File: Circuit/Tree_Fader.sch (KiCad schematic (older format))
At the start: 20 parts

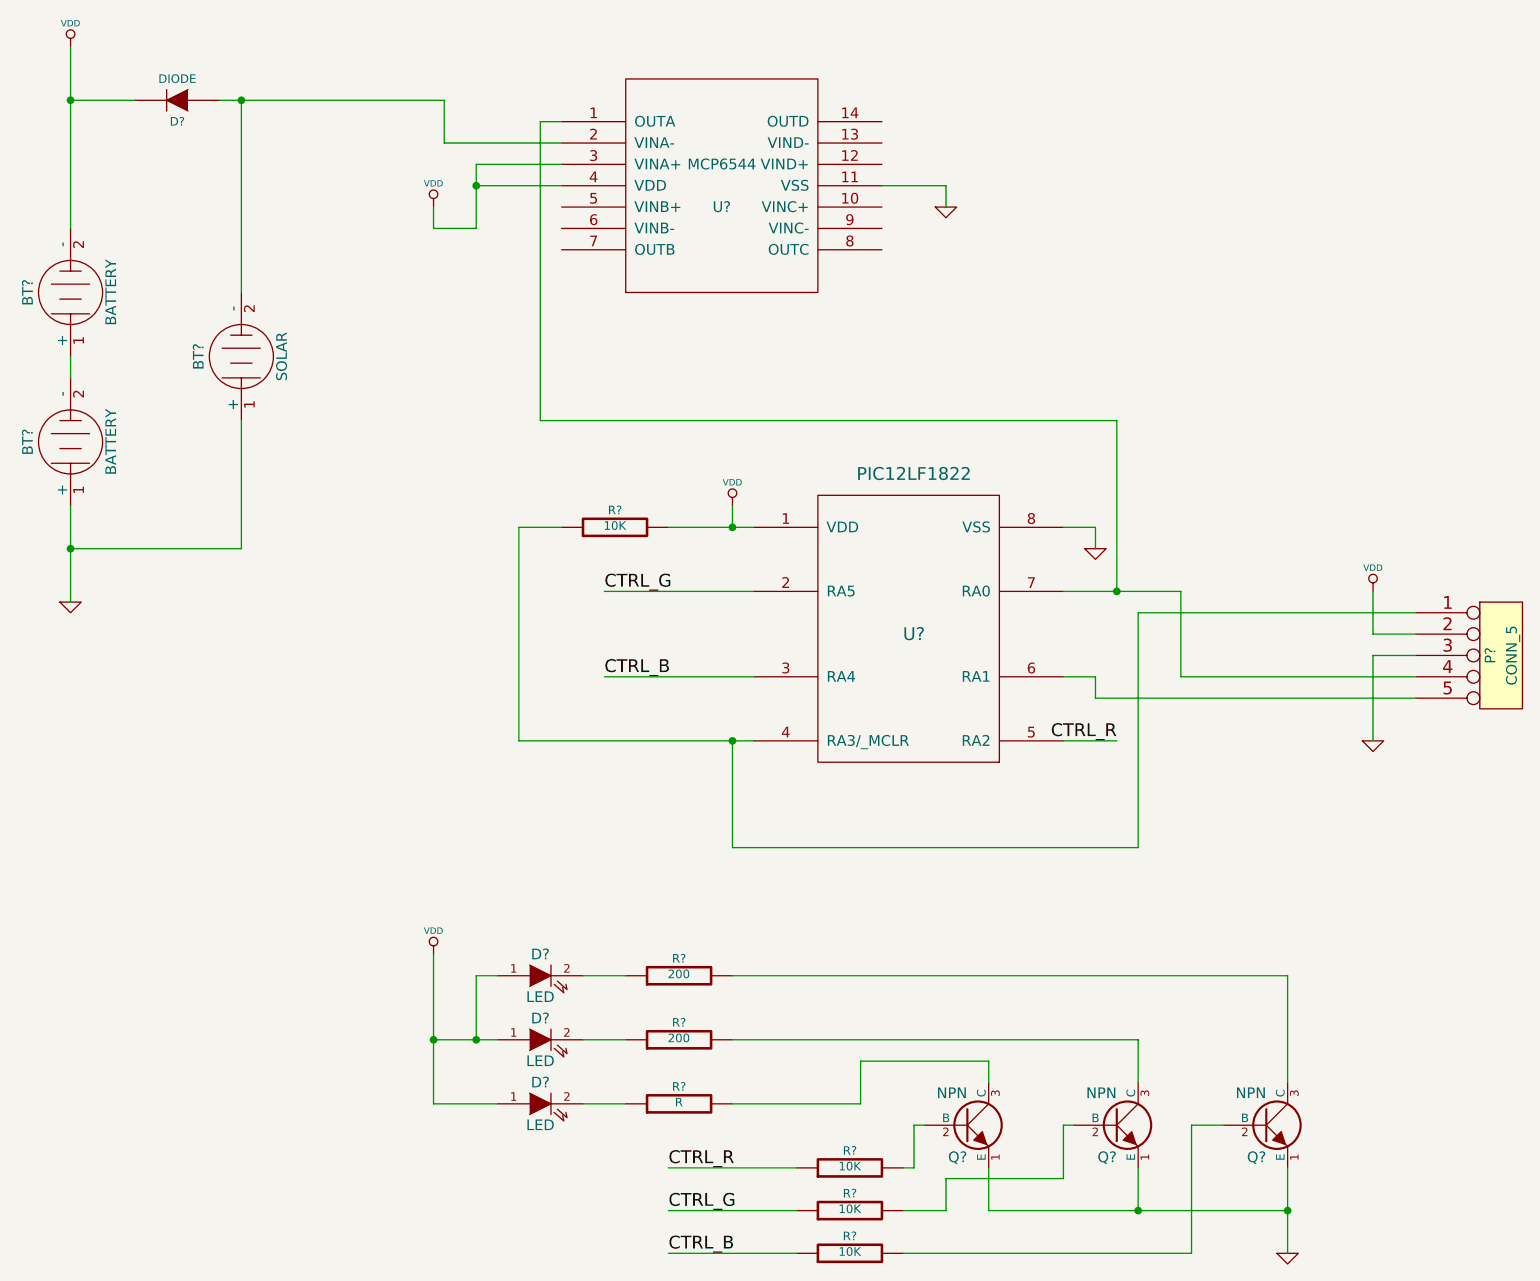
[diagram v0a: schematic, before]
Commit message: Created PCB in KiCad
Submitted order to OSH Park.  Of course, resistors R4 and R3 are not
connected to the ground of D4 and D3.  This is fixed here, but the order
was submitted, and will require a "bodge wire".
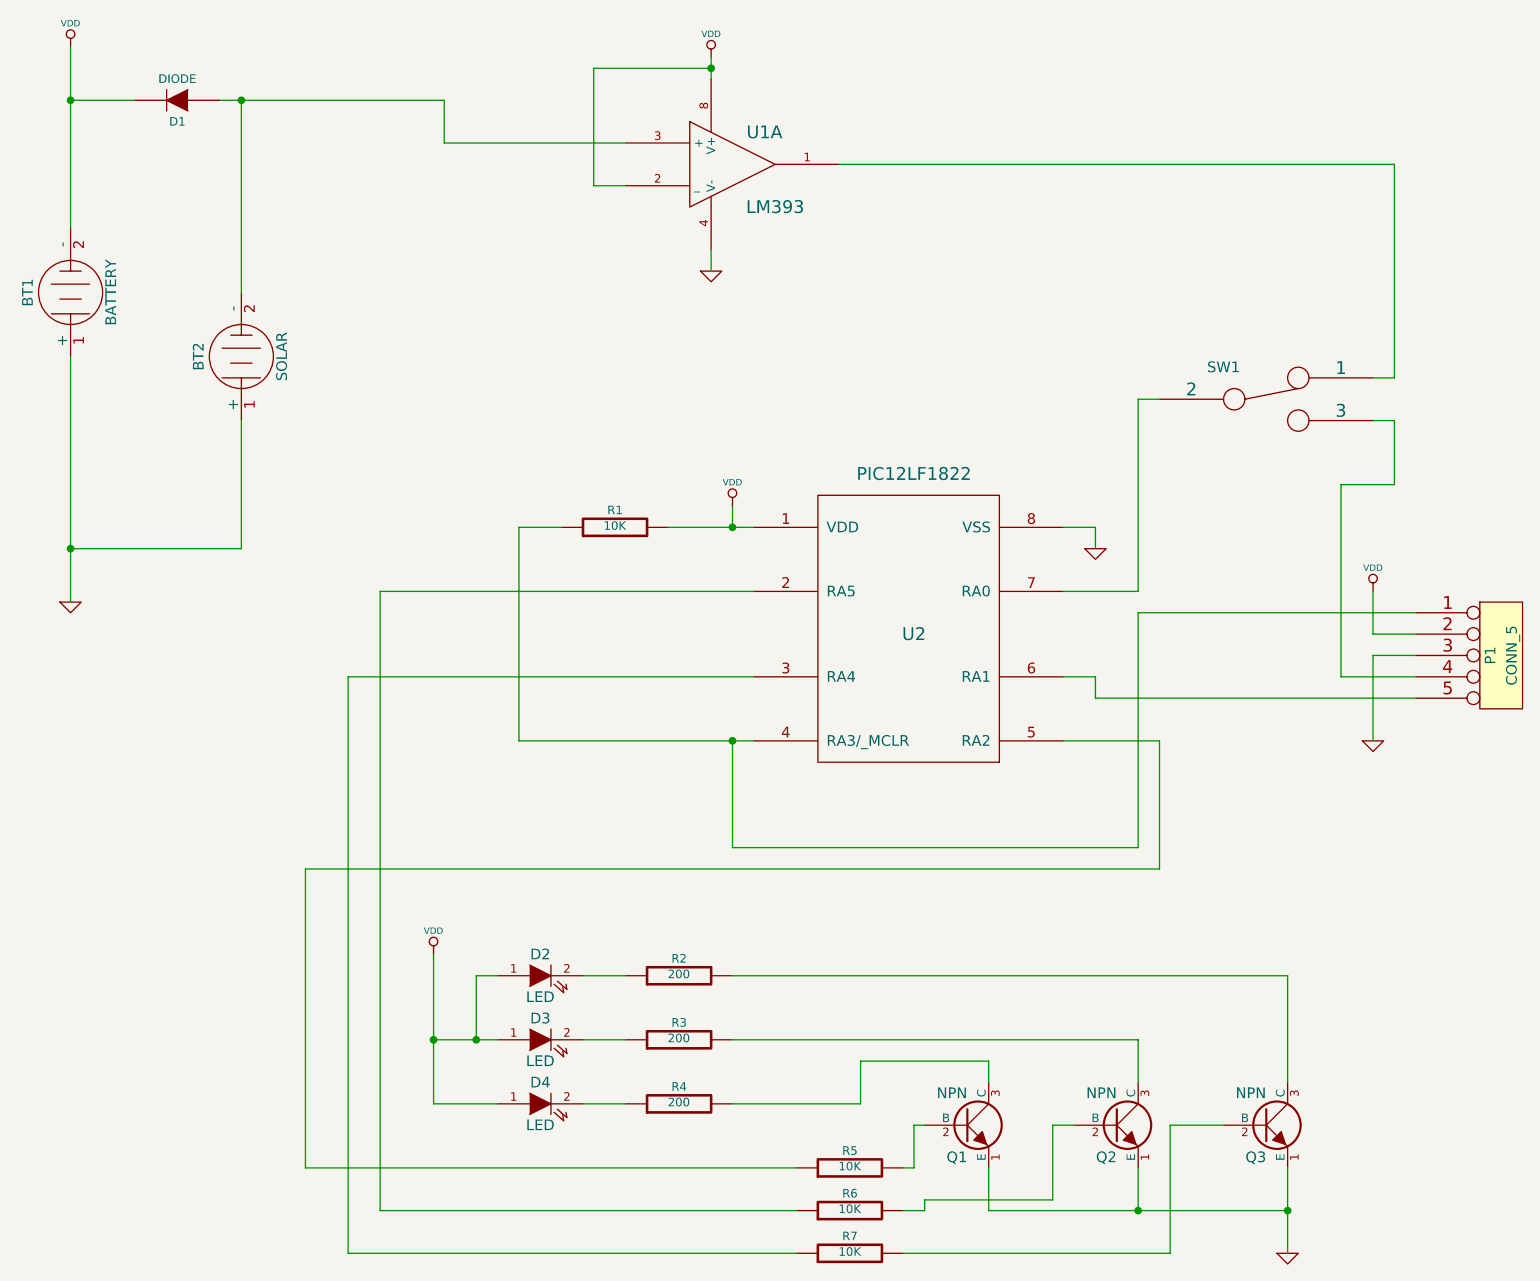
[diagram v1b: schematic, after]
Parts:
- removed BT?: BATTERY, ~, symbol BATTERY
- removed U?: MCP6544, MODULE, symbol MCP6544
- added SW1: (no value), ~, symbol SWITCH_INV
- added U1: LM393, symbol LM393
- R4: renamed from R?; value R -> 200
- gave numbers to parts that had none: 17
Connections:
- net GND: now also BT1.1 (+), U1.4 (V-)
- net VDD: now also U1.2 (_), U1.8 (V+)
- net at U2.7 (RA0): now also SW1.2; no longer P1.4
- net at BT2.2 (-), D1.1 (A): now also U1.3 (+)
- net CTRL_B: no longer names the net of R7.1, U2.3 (RA4)
- net CTRL_G: no longer names the net of R6.1, U2.2 (RA5)
- net CTRL_R: no longer names the net of R5.1, U2.5 (RA2)
- new net: P1.4, SW1.3
- new net: SW1.1, U1.1
